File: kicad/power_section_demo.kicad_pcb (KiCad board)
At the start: 2 copper layers, 120 x 70 mm, 8 parts, among them U1 LM317T

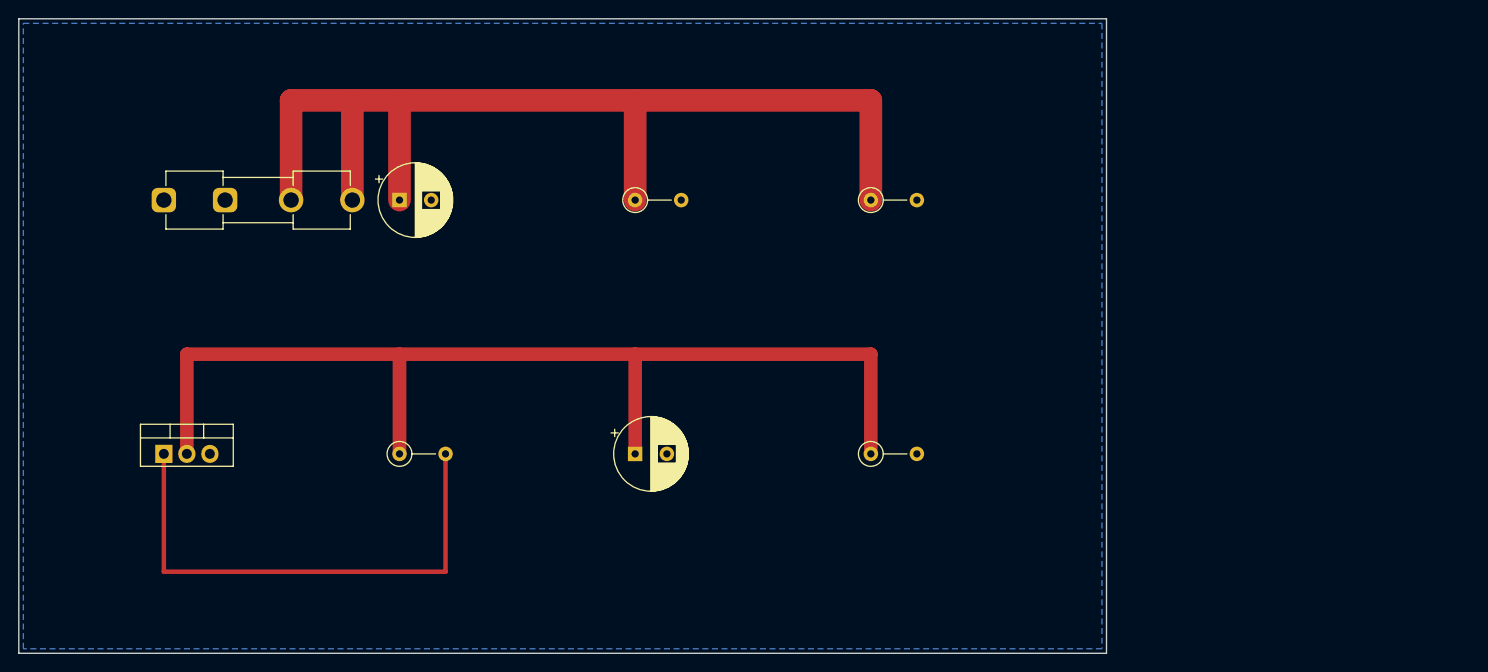
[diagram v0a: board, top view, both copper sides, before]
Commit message: Datasheet footprints, floor-plan placement, headless autoroute (144/145, DRC 0)
PCB-AUDIT s1 fixes with datasheet-derived project footprints:
- TO-220-5_Vertical_P1.70mm_LM1875 (TI NDH0005D): 1.45 mm pads on the 1.1 mm
  drill -> 0.175 mm annular (was 0.0875, 5 DRC errors); pad-local 0.2 mm clearance
- Bridge_KBP_P3.81mm (Diodes DS39310 KBP404G-KBP410G, pins + ~ ~ -); bridge
  symbol renumbered to the physical order; errata #3 updated (KBU needs a swap)
- value-aware CP/R sizing (real can sizes for 4700/2200/1000 uF, 5 W / 1 W
  resistors, fat pads on the 0R speaker return); Part 4 wire pads for all
  off-board wiring (2.0 mm/1.2 mm signal, 3.0 mm/1.5 mm speaker + transformer)
- VRAW/AC1/AC2 moved into the HighCurrent net class (errata #11)

gen_pcb.py now places to the Part 5 floor plan: balanced columns (Input/Preamp
with Tone stacked below | Reverb/Trem/MRB | Power Amp | PSU), signal order inside
zones with serpentine shelves, LM1875/LM317 on the top edge with the 10 mm
keep-out, wiring edge along the bottom, 4x M3 holes, two locked 0.9 mm escape
stubs off the LM1875 pins 4/5 (a 1.5/2.5 mm trace cannot enter a 1.70 mm pitch).
DRC before routing: 0 errors, 0 warnings.

route_board.py: pcbnew DSN export -> Freerouting -> SES import -> pour refill.
Freerouting 2.1.0 ignores every pass/timeout limit in CLI mode and only writes
output at 0 unrouted (and its MT router crashed), so the script drives 1.9.0
under xvfb-run and injects autoroute_settings (bottom layer 6x cost, via 80) so
the GND pour stays whole. Committed board: 144/145 connections routed, 0 DRC
violations (--severity-all), 26 vias, 351 mm on the bottom vs 3.7 m on top; the
one open PA_OUT link (blocked by R_bias1) is documented as a GUI finish.

Chassis-fit figure corrected: the old 48-53 % / 82-90 % densities counted hidden
text boxes; text-less it is ~33 % on 190x115 and ~56 % on 155x90.

Docs: PCB-NOTES/PCB-AUDIT rewritten, README, CHANGELOG, errata #3/#11,
SOURCES (package drawings), Part 10, kicad RE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
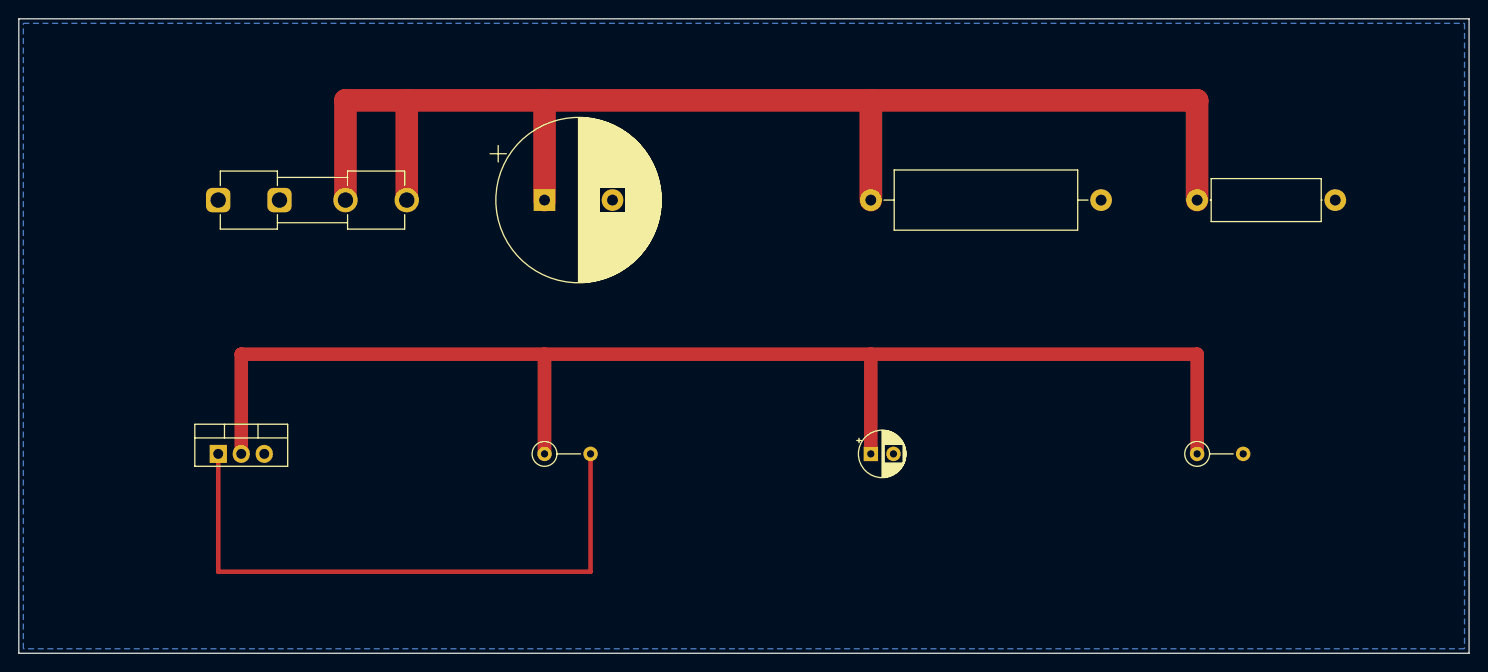
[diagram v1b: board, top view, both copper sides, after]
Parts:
- removed the C_main at (42.0, 20.0)
- removed the R_27V at (94.0, 20.0)
- removed the R_bleed at (68.0, 20.0)
- added C_main: 4700uF/50V, CP_Radial_D18.0mm_P7.50mm, F.Cu at (58.0, 20.0)
- added R_27V: 100R/1W, R_Axial_DIN0414_L11.9mm_D4.5mm_P15.24mm_Horizontal, F.Cu at (130.0, 20.0)
- added R_bleed: 10k/5W, R_Axial_Power_L20.0mm_W6.4mm_P25.40mm, F.Cu at (94.0, 20.0)
- C_reg_out1: footprint CP_Radial_D8.0mm_P3.50mm -> CP_Radial_D5.0mm_P2.50mm
- moved R_vbr1 36.0 mm to (130.0, 48.0)
- moved C_reg_out1 26.0 mm to (94.0, 48.0)
- moved R_reg1 16.0 mm to (58.0, 48.0)
- moved F1 6.00 mm to (22.0, 20.0)
- moved U1 6.00 mm to (22.0, 48.0)
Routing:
- net +33V5: track 119.0 -> 149.0 mm
- net +17V: track 119.5 -> 149.5 mm
- net ADJ17: track 57.1 -> 67.1 mm
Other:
- board size 120 x 70 mm -> 160 x 70 mm
